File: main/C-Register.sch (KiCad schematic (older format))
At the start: 19 parts, among them U80 74LS245, U81 74LS173, U82 74LS173

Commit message: Replot main with symbols
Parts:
- renumbered D70 to D62, D71 to D63, D72 to D64, D73 to D65, D74 to D66, D75 to D67, D76 to D68, D77 to D69, R76 to R68, R77 to R69, R78 to R70, R79 to R71, R80 to R72, R81 to R73, R82 to R74, R83 to R75, U80 to U65, U81 to U66, U82 to U67
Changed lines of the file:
@@
 Sheet 18 26
 Title "C Register"
-Date "2019-11-13"
+Date "2019-11-17"
 Rev "v1.0"
 Comp "Christopher Milan"
@@
 AR Path="/5D9C722C/5D9DFD2F" Ref="U?"  Part="1"
 AR Path="/5D9DCC2F/5D9DFD2F" Ref="U?"  Part="1"
-AR Path="/5DA98D6D/5DA9A59D/5D9DFD2F" Ref="U80"  Part="1"
-F 0 "U80" V 3396 1956 50  0000 R CNN
+AR Path="/5DA98D6D/5DA9A59D/5D9DFD2F" Ref="U65"  Part="1"
+F 0 "U65" V 3396 1956 50  0000 R CNN
 F 1 "74LS245" V 3305 1956 50  0000 R CNN
 F 2 "" H 3350 2800 50  0001 C CNN
@@
 AR Path="/5D9C722C/5D9DFD5C" Ref="U?"  Part="1"
 AR Path="/5D9DCC2F/5D9DFD5C" Ref="U?"  Part="1"
-AR Path="/5DA98D6D/5DA9A59D/5D9DFD5C" Ref="U82"  Part="1"
-F 0 "U82" V 7904 3744 50  0000 L CNN
+AR Path="/5DA98D6D/5DA9A59D/5D9DFD5C" Ref="U67"  Part="1"
+F 0 "U67" V 7904 3744 50  0000 L CNN
 F 1 "74LS173" V 7995 3744 50  0000 L CNN
 F 2 "" H 7950 2800 50  0001 C CNN
@@
 AR Path="/5D9C722C/5D9DFD86" Ref="D?"  Part="1"
 AR Path="/5D9DCC2F/5D9DFD86" Ref="D?"  Part="1"
-AR Path="/5DA98D6D/5DA9A59D/5D9DFD86" Ref="D70"  Part="1"
-F 0 "D70" V 3939 5183 50  0000 R CNN
+AR Path="/5DA98D6D/5DA9A59D/5D9DFD86" Ref="D62"  Part="1"
+F 0 "D62" V 3939 5183 50  0000 R CNN
 F 1 "LED" V 3848 5183 50  0000 R CNN
 F 2 "" H 3900 5300 50  0001 C CNN
@@
 AR Path="/5D9C722C/5D9DFD8C" Ref="D?"  Part="1"
 AR Path="/5D9DCC2F/5D9DFD8C" Ref="D?"  Part="1"
-AR Path="/5DA98D6D/5DA9A59D/5D9DFD8C" Ref="D71"  Part="1"
-F 0 "D71" V 4289 5183 50  0000 R CNN
+AR Path="/5DA98D6D/5DA9A59D/5D9DFD8C" Ref="D63"  Part="1"
+F 0 "D63" V 4289 5183 50  0000 R CNN
 F 1 "LED" V 4198 5183 50  0000 R CNN
 F 2 "" H 4250 5300 50  0001 C CNN
@@
 AR Path="/5D9C722C/5D9DFD92" Ref="D?"  Part="1"
 AR Path="/5D9DCC2F/5D9DFD92" Ref="D?"  Part="1"
-AR Path="/5DA98D6D/5DA9A59D/5D9DFD92" Ref="D72"  Part="1"
-F 0 "D72" V 4639 5183 50  0000 R CNN
+AR Path="/5DA98D6D/5DA9A59D/5D9DFD92" Ref="D64"  Part="1"
+F 0 "D64" V 4639 5183 50  0000 R CNN
 F 1 "LED" V 4548 5183 50  0000 R CNN
 F 2 "" H 4600 5300 50  0001 C CNN
@@
 AR Path="/5D9C722C/5D9DFD98" Ref="D?"  Part="1"
 AR Path="/5D9DCC2F/5D9DFD98" Ref="D?"  Part="1"
-AR Path="/5DA98D6D/5DA9A59D/5D9DFD98" Ref="D73"  Part="1"
-F 0 "D73" V 4989 5183 50  0000 R CNN
+AR Path="/5DA98D6D/5DA9A59D/5D9DFD98" Ref="D65"  Part="1"
+F 0 "D65" V 4989 5183 50  0000 R CNN
 F 1 "LED" V 4898 5183 50  0000 R CNN
 F 2 "" H 4950 5300 50  0001 C CNN
@@
 AR Path="/5D9C722C/5D9DFD9E" Ref="D?"  Part="1"
 AR Path="/5D9DCC2F/5D9DFD9E" Ref="D?"  Part="1"
-AR Path="/5DA98D6D/5DA9A59D/5D9DFD9E" Ref="D74"  Part="1"
-F 0 "D74" V 5339 5183 50  0000 R CNN
+AR Path="/5DA98D6D/5DA9A59D/5D9DFD9E" Ref="D66"  Part="1"
+F 0 "D66" V 5339 5183 50  0000 R CNN
 F 1 "LED" V 5248 5183 50  0000 R CNN
 F 2 "" H 5300 5300 50  0001 C CNN
@@
 AR Path="/5D9C722C/5D9DFDA4" Ref="D?"  Part="1"
 AR Path="/5D9DCC2F/5D9DFDA4" Ref="D?"  Part="1"
-AR Path="/5DA98D6D/5DA9A59D/5D9DFDA4" Ref="D75"  Part="1"
-F 0 "D75" V 5689 5183 50  0000 R CNN
+AR Path="/5DA98D6D/5DA9A59D/5D9DFDA4" Ref="D67"  Part="1"
+F 0 "D67" V 5689 5183 50  0000 R CNN
 F 1 "LED" V 5598 5183 50  0000 R CNN
 F 2 "" H 5650 5300 50  0001 C CNN
@@
 AR Path="/5D9C722C/5D9DFDAA" Ref="D?"  Part="1"
 AR Path="/5D9DCC2F/5D9DFDAA" Ref="D?"  Part="1"
-AR Path="/5DA98D6D/5DA9A59D/5D9DFDAA" Ref="D76"  Part="1"
-F 0 "D76" V 6039 5183 50  0000 R CNN
+AR Path="/5DA98D6D/5DA9A59D/5D9DFDAA" Ref="D68"  Part="1"
+F 0 "D68" V 6039 5183 50  0000 R CNN
 F 1 "LED" V 5948 5183 50  0000 R CNN
 F 2 "" H 6000 5300 50  0001 C CNN
@@
 AR Path="/5D9C722C/5D9DFDB0" Ref="D?"  Part="1"
 AR Path="/5D9DCC2F/5D9DFDB0" Ref="D?"  Part="1"
-AR Path="/5DA98D6D/5DA9A59D/5D9DFDB0" Ref="D77"  Part="1"
-F 0 "D77" V 6389 5183 50  0000 R CNN
+AR Path="/5DA98D6D/5DA9A59D/5D9DFDB0" Ref="D69"  Part="1"
+F 0 "D69" V 6389 5183 50  0000 R CNN
 F 1 "LED" V 6298 5183 50  0000 R CNN
 F 2 "" H 6350 5300 50  0001 C CNN
@@
 AR Path="/5D9C722C/5D9DFDCC" Ref="R?"  Part="1"
 AR Path="/5D9DCC2F/5D9DFDCC" Ref="R?"  Part="1"
-AR Path="/5DA98D6D/5DA9A59D/5D9DFDCC" Ref="R76"  Part="1"
-F 0 "R76" H 3970 5896 50  0000 L CNN
+AR Path="/5DA98D6D/5DA9A59D/5D9DFDCC" Ref="R68"  Part="1"
+F 0 "R68" H 3970 5896 50  0000 L CNN
 F 1 "220" H 3970 5805 50  0000 L CNN
 F 2 "" V 3830 5850 50  0001 C CNN
@@
 AR Path="/5D9C722C/5D9DFDD2" Ref="R?"  Part="1"
 AR Path="/5D9DCC2F/5D9DFDD2" Ref="R?"  Part="1"
-AR Path="/5DA98D6D/5DA9A59D/5D9DFDD2" Ref="R77"  Part="1"
-F 0 "R77" H 4320 5896 50  0000 L CNN
+AR Path="/5DA98D6D/5DA9A59D/5D9DFDD2" Ref="R69"  Part="1"
+F 0 "R69" H 4320 5896 50  0000 L CNN
 F 1 "220" H 4320 5805 50  0000 L CNN
 F 2 "" V 4180 5850 50  0001 C CNN
@@
 AR Path="/5D9C722C/5D9DFDD8" Ref="R?"  Part="1"
 AR Path="/5D9DCC2F/5D9DFDD8" Ref="R?"  Part="1"
-AR Path="/5DA98D6D/5DA9A59D/5D9DFDD8" Ref="R78"  Part="1"
-F 0 "R78" H 4670 5896 50  0000 L CNN
+AR Path="/5DA98D6D/5DA9A59D/5D9DFDD8" Ref="R70"  Part="1"
+F 0 "R70" H 4670 5896 50  0000 L CNN
 F 1 "220" H 4670 5805 50  0000 L CNN
 F 2 "" V 4530 5850 50  0001 C CNN
@@
 AR Path="/5D9C722C/5D9DFDDE" Ref="R?"  Part="1"
 AR Path="/5D9DCC2F/5D9DFDDE" Ref="R?"  Part="1"
-AR Path="/5DA98D6D/5DA9A59D/5D9DFDDE" Ref="R79"  Part="1"
-F 0 "R79" H 5020 5896 50  0000 L CNN
+AR Path="/5DA98D6D/5DA9A59D/5D9DFDDE" Ref="R71"  Part="1"
+F 0 "R71" H 5020 5896 50  0000 L CNN
 F 1 "220" H 5020 5805 50  0000 L CNN
 F 2 "" V 4880 5850 50  0001 C CNN
@@
 AR Path="/5D9C722C/5D9DFDE4" Ref="R?"  Part="1"
 AR Path="/5D9DCC2F/5D9DFDE4" Ref="R?"  Part="1"
-AR Path="/5DA98D6D/5DA9A59D/5D9DFDE4" Ref="R80"  Part="1"
-F 0 "R80" H 5370 5896 50  0000 L CNN
+AR Path="/5DA98D6D/5DA9A59D/5D9DFDE4" Ref="R72"  Part="1"
+F 0 "R72" H 5370 5896 50  0000 L CNN
 F 1 "220" H 5370 5805 50  0000 L CNN
 F 2 "" V 5230 5850 50  0001 C CNN
@@
 AR Path="/5D9C722C/5D9DFDEA" Ref="R?"  Part="1"
 AR Path="/5D9DCC2F/5D9DFDEA" Ref="R?"  Part="1"
-AR Path="/5DA98D6D/5DA9A59D/5D9DFDEA" Ref="R81"  Part="1"
-F 0 "R81" H 5720 5896 50  0000 L CNN
+AR Path="/5DA98D6D/5DA9A59D/5D9DFDEA" Ref="R73"  Part="1"
+F 0 "R73" H 5720 5896 50  0000 L CNN
 F 1 "220" H 5720 5805 50  0000 L CNN
 F 2 "" V 5580 5850 50  0001 C CNN
@@
 AR Path="/5D9C722C/5D9DFDF0" Ref="R?"  Part="1"
 AR Path="/5D9DCC2F/5D9DFDF0" Ref="R?"  Part="1"
-AR Path="/5DA98D6D/5DA9A59D/5D9DFDF0" Ref="R82"  Part="1"
-F 0 "R82" H 6070 5896 50  0000 L CNN
+AR Path="/5DA98D6D/5DA9A59D/5D9DFDF0" Ref="R74"  Part="1"
+F 0 "R74" H 6070 5896 50  0000 L CNN
 F 1 "220" H 6070 5805 50  0000 L CNN
 F 2 "" V 5930 5850 50  0001 C CNN
@@
 AR Path="/5D9C722C/5D9DFDF6" Ref="R?"  Part="1"
 AR Path="/5D9DCC2F/5D9DFDF6" Ref="R?"  Part="1"
-AR Path="/5DA98D6D/5DA9A59D/5D9DFDF6" Ref="R83"  Part="1"
-F 0 "R83" H 6420 5896 50  0000 L CNN
+AR Path="/5DA98D6D/5DA9A59D/5D9DFDF6" Ref="R75"  Part="1"
+F 0 "R75" H 6420 5896 50  0000 L CNN
 F 1 "220" H 6420 5805 50  0000 L CNN
 F 2 "" V 6280 5850 50  0001 C CNN
@@
 AR Path="/5D9C722C/5D9DFE47" Ref="U?"  Part="1"
 AR Path="/5D9DCC2F/5D9DFE47" Ref="U?"  Part="1"
-AR Path="/5DA98D6D/5DA9A59D/5D9DFE47" Ref="U81"  Part="1"
-F 0 "U81" V 5654 3744 50  0000 L CNN
+AR Path="/5DA98D6D/5DA9A59D/5D9DFE47" Ref="U66"  Part="1"
+F 0 "U66" V 5654 3744 50  0000 L CNN
 F 1 "74LS173" V 5745 3744 50  0000 L CNN
 F 2 "" H 5700 2800 50  0001 C CNN

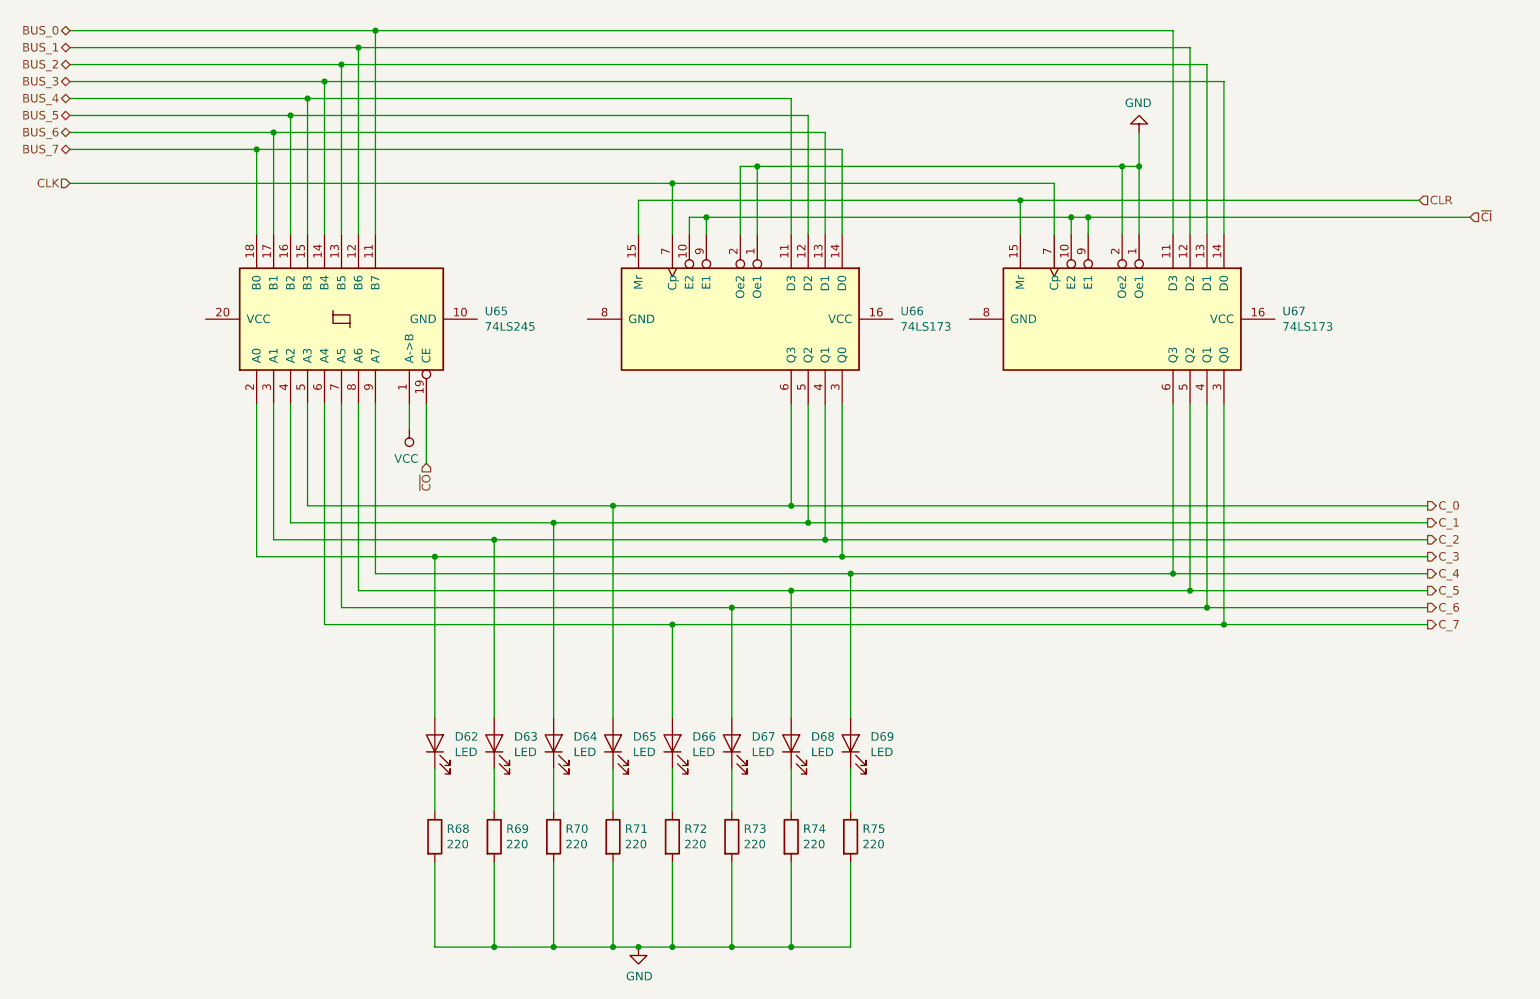
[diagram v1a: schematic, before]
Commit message: Switch to using 74LS377 in place of two 74LS173
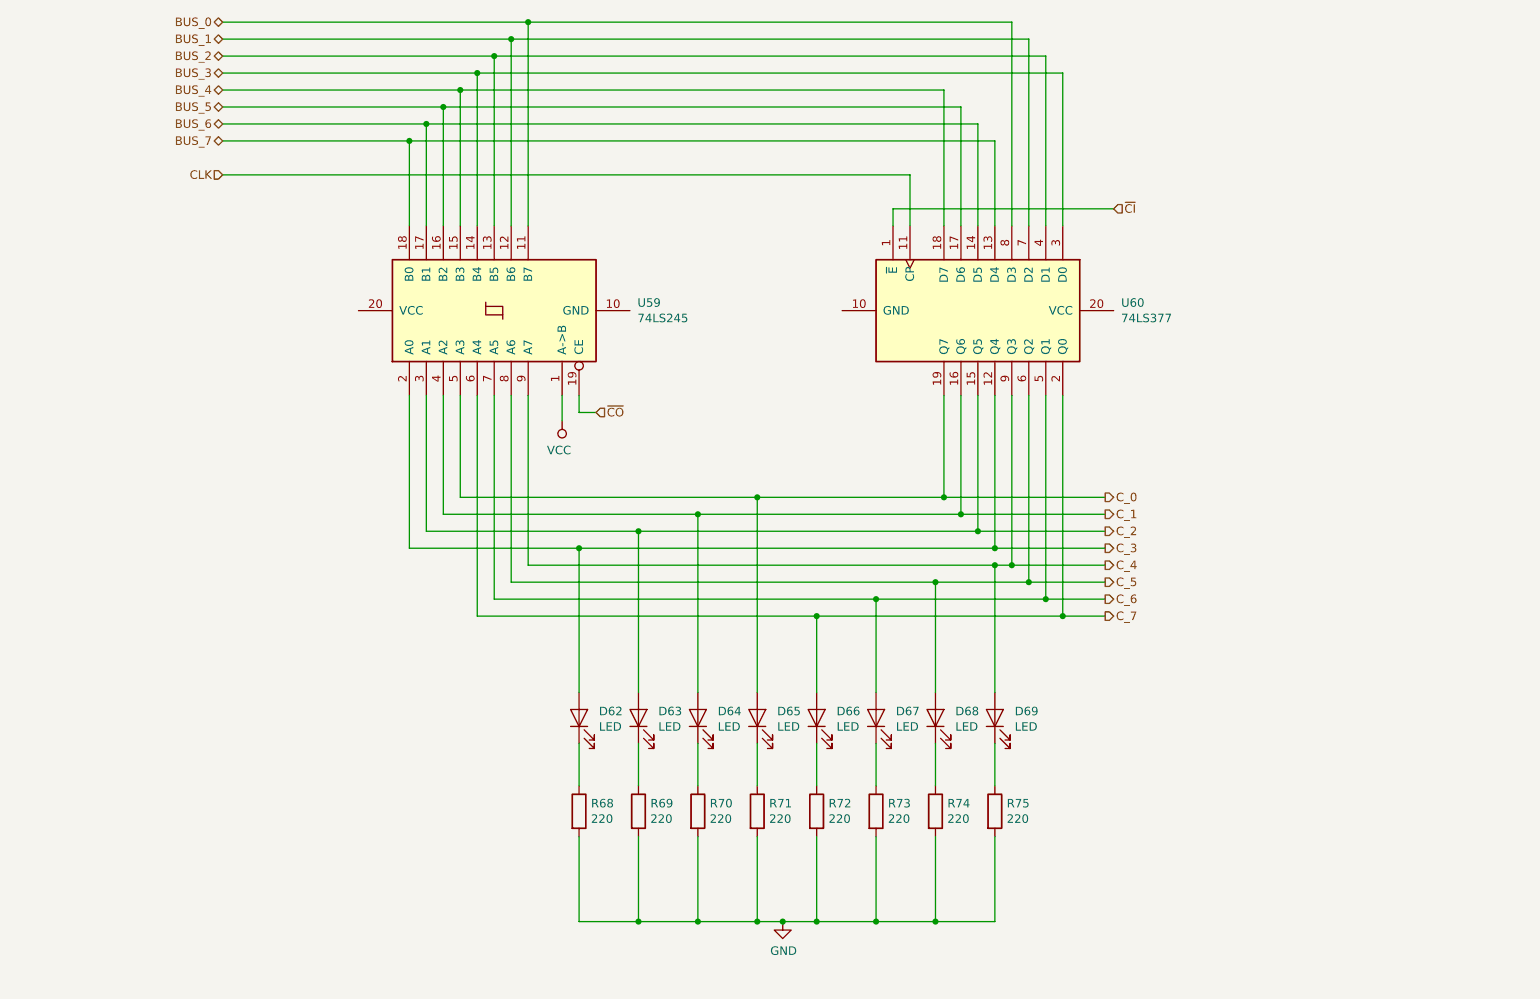
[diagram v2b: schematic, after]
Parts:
- removed U65: 74LS245, symbol 74xx:74LS245
- removed U66, U67: 74LS173, symbol 74xx:74LS173
- added U59: 74LS245, symbol 74xx:74LS245
- added U60: 74LS377, symbol 74xx:74LS377
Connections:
- net BUS_0: now also U59.11 (B7), U60.8 (D3)
- net BUS_1: now also U59.12 (B6), U60.7 (D2)
- net BUS_2: now also U59.13 (B5), U60.4 (D1)
- net BUS_3: now also U59.14 (B4), U60.3 (D0)
- net BUS_4: now also U59.15 (B3), U60.18 (D7)
- net BUS_5: now also U59.16 (B2), U60.17 (D6)
- net BUS_6: now also U59.17 (B1), U60.14 (D5)
- net BUS_7: now also U59.18 (B0), U60.13 (D4)
- net CLK: now also U60.11 (CP)
- net C_0: now also U59.5 (A3), U60.19 (Q7)
- net C_1: now also U59.4 (A2), U60.16 (Q6)
- net C_2: now also U59.3 (A1), U60.15 (Q5)
- net C_3: now also U59.2 (A0), U60.12 (Q4)
- net C_4: now also U59.9 (A7), U60.9 (Q3)
- net C_5: now also U59.8 (A6), U60.6 (Q2)
- net C_6: now also U59.7 (A5), U60.5 (Q1)
- net C_7: now also U59.6 (A4), U60.2 (Q0)
- net VCC: now also U59.1 (A->B)
- net ~CI~: now also U60.1 (~E)
- net ~CO~: now also U59.19 (CE)
